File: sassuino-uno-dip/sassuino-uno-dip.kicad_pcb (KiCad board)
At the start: 2 copper layers, 68.6 x 53.3 mm, 33 parts, among them J1 USB_B, J10 OSCPWR_HDR, J2 POWER2_HDR, J3 ICSP_HDR, J4 POWER_HDR, J5 PORTC_HDR, J6 PORTB_HDR, J7 PORTD_HDR, J8 XTAL2_HDR, J9 XTAL1_HDR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

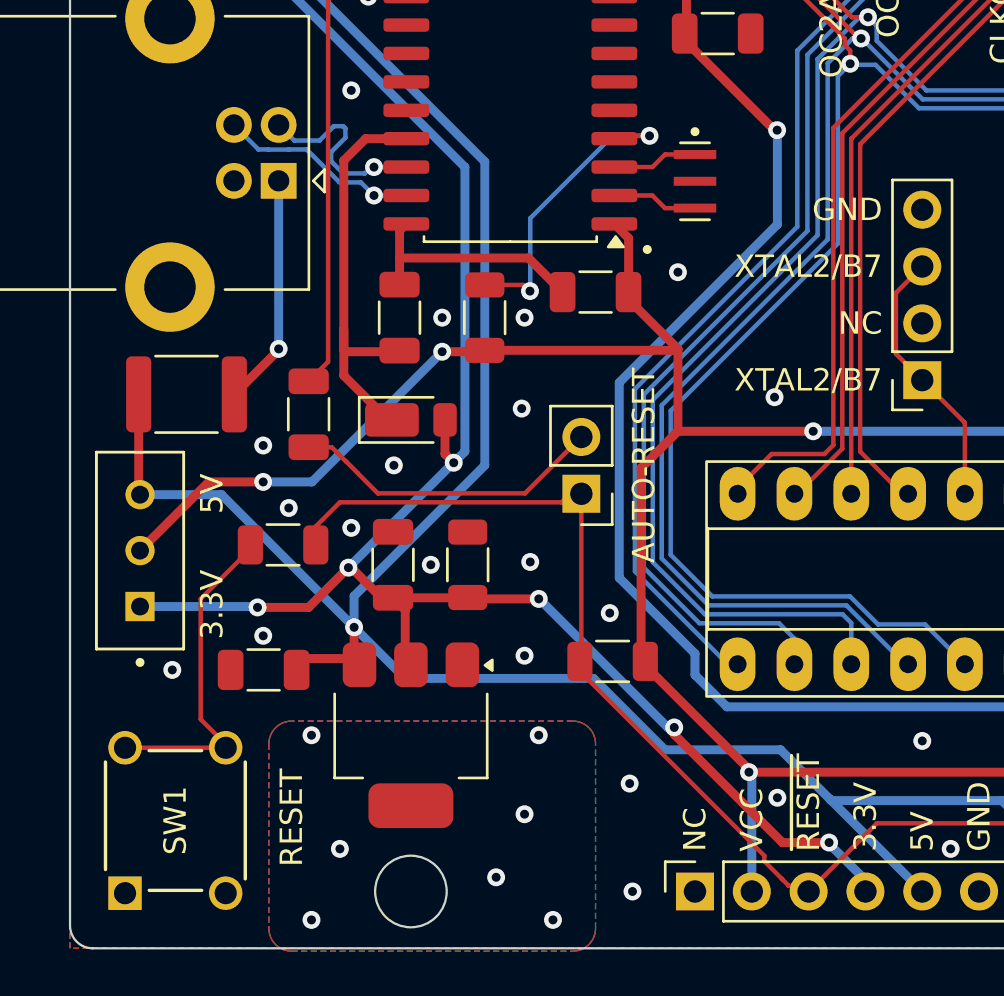
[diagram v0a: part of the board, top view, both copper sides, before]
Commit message: Remove the diode between the two LDOs, I don't remember why it was there.
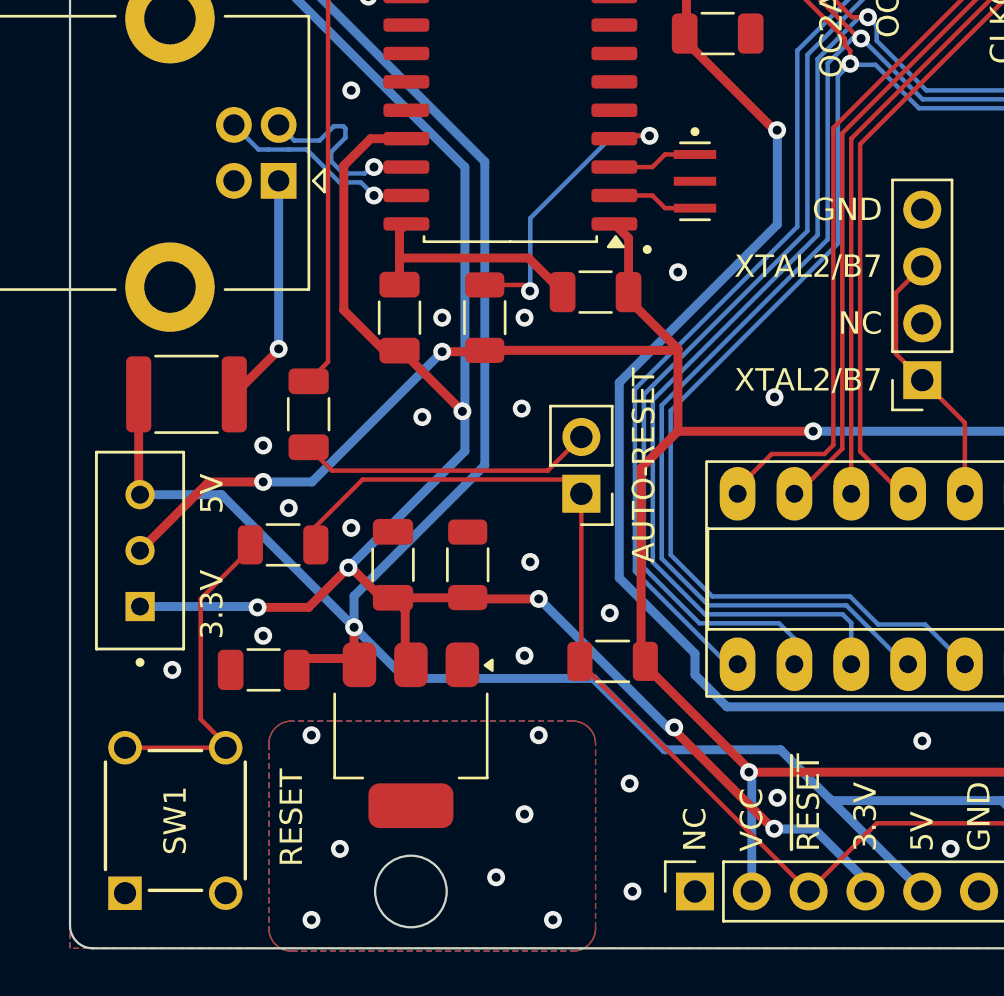
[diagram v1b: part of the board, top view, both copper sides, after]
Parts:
- removed D1: DFLS130L-7, Diode_SMD:D_PowerDI-123
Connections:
- C3 pad 1: /VUSB -> +3.3V
- U2 pad 17: /VUSB -> +3.3V
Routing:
- net /VUSB: track 18.5 -> 0.00 mm
- net +3.3V: track 85.9 -> 100.6 mm
- net Net-(JP2-B): track 14.1 -> 13.2 mm
- net GND: vias 49 -> 48

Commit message: Replace crystal header 3d model with the part I'll likely be using.
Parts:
- J10, J8, J9: footprint Connector_PinSocket_2.54mm:PinSocket_1x04_P2.54mm_Vertical -> 0SassuinoFP:PinSocket_1x04_P2.54mm_Vertical_LowProfile
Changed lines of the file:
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@@
 	(net 50 "/RESET_SW")
 	(net 51 "/VBUS")
-	(footprint "Connector_PinSocket_2.54mm:PinSocket_1x04_P2.54mm_Vertical"
+	(footprint "0SassuinoFP:PinSocket_1x04_P2.54mm_Vertical_LowProfile"
 		(layer "F.Cu")
 		(at 88.9 129.54 180)
@@
 		(tags "Through hole socket strip THT 1x04 2.54mm single row")
 		(property "Reference" "J8"
-			(at 0 10.414 0)
+			(at 0 -2.77 180)
 			(layer "F.SilkS")
-			(hide yes)
 			(effects
 				(font
@@
 		)
 		(property "Value" "XTAL2_HDR"
-			(at 0 10.39 0)
+			(at 0 10.39 180)
 			(layer "F.Fab")
 			(effects
@@
 		)
 		(fp_text user "${REFERENCE}"
-			(at 0 3.81 90)
+			(at 0 3.81 270)
 			(layer "F.Fab")
 			(effects
@@
 		)
 		(embedded_fonts no)
-		(model "${KICAD6_3DMODEL_DIR}/Connector_PinSocket_2.54mm.3dshapes/PinSocket_1x04_P2.54mm_Vertical.wrl"
+		(model "${KIPRJMOD}/../lib/0Sassuino3D/315-47-104-41-001000.STEP"
 			(offset
-				(xyz 0 0 0)
+				(xyz 0 -7.5 3)
 			)
 			(scale
@@
 			)
 			(rotate
-				(xyz 0 0 0)
+				(xyz -90 -0 -90)
 			)
 		)
@@
 		)
 	)
-	(footprint "Connector_PinSocket_2.54mm:PinSocket_1x04_P2.54mm_Vertical"
+	(footprint "0SassuinoFP:PinSocket_1x04_P2.54mm_Vertical_LowProfile"
 		(layer "F.Cu")
 		(at 93.98 129.54 180)
@@
 		(tags "Through hole socket strip THT 1x04 2.54mm single row")
 		(property "Reference" "J9"
-			(at 0 10.414 0)
+			(at 0 -2.77 180)
 			(layer "F.SilkS")
-			(hide yes)
 			(effects
 				(font
@@
 		)
 		(property "Value" "XTAL1_HDR"
-			(at 0 10.39 0)
+			(at 0 10.39 180)
 			(layer "F.Fab")
 			(effects
@@
 		)
 		(fp_text user "${REFERENCE}"
-			(at 0 3.81 90)
+			(at 0 3.81 270)
 			(layer "F.Fab")
 			(effects
@@
 		)
 		(embedded_fonts no)
-		(model "${KICAD6_3DMODEL_DIR}/Connector_PinSocket_2.54mm.3dshapes/PinSocket_1x04_P2.54mm_Vertical.wrl"
+		(model "${KIPRJMOD}/../lib/0Sassuino3D/315-47-104-41-001000.STEP"
 			(offset
-				(xyz 0 0 0)
+				(xyz 0 -7.5 3)
 			)
 			(scale
@@
 			)
 			(rotate
-				(xyz 0 0 0)
+				(xyz -90 -0 -90)
 			)
 		)
 	)
-	(footprint "Connector_PinSocket_2.54mm:PinSocket_1x04_P2.54mm_Vertical"
+	(footprint "0SassuinoFP:PinSocket_1x04_P2.54mm_Vertical_LowProfile"
 		(layer "F.Cu")
 		(at 109.22 129.54 180)
@@
 		(tags "Through hole socket strip THT 1x04 2.54mm single row")
 		(property "Reference" "J10"
-			(at -0.127 10.414 0)
+			(at 0 -2.77 180)
 			(layer "F.SilkS")
-			(hide yes)
 			(effects
 				(font
@@
 		)
 		(property "Value" "OSCPWR_HDR"
-			(at 0 10.39 0)
+			(at 0 10.39 180)
 			(layer "F.Fab")
 			(effects
@@
 		)
 		(fp_text user "${REFERENCE}"
-			(at 0 3.81 90)
+			(at 0 3.81 270)
 			(layer "F.Fab")
 			(effects
@@
 		)
 		(embedded_fonts no)
-		(model "${KICAD6_3DMODEL_DIR}/Connector_PinSocket_2.54mm.3dshapes/PinSocket_1x04_P2.54mm_Vertical.wrl"
+		(model "${KIPRJMOD}/../lib/0Sassuino3D/315-47-104-41-001000.STEP"
 			(offset
-				(xyz 0 0 0)
+				(xyz 0 -7.5 3)
 			)
 			(scale
@@
 			)
 			(rotate
-				(xyz 0 0 0)
+				(xyz -90 -0 -90)
 			)
 		)

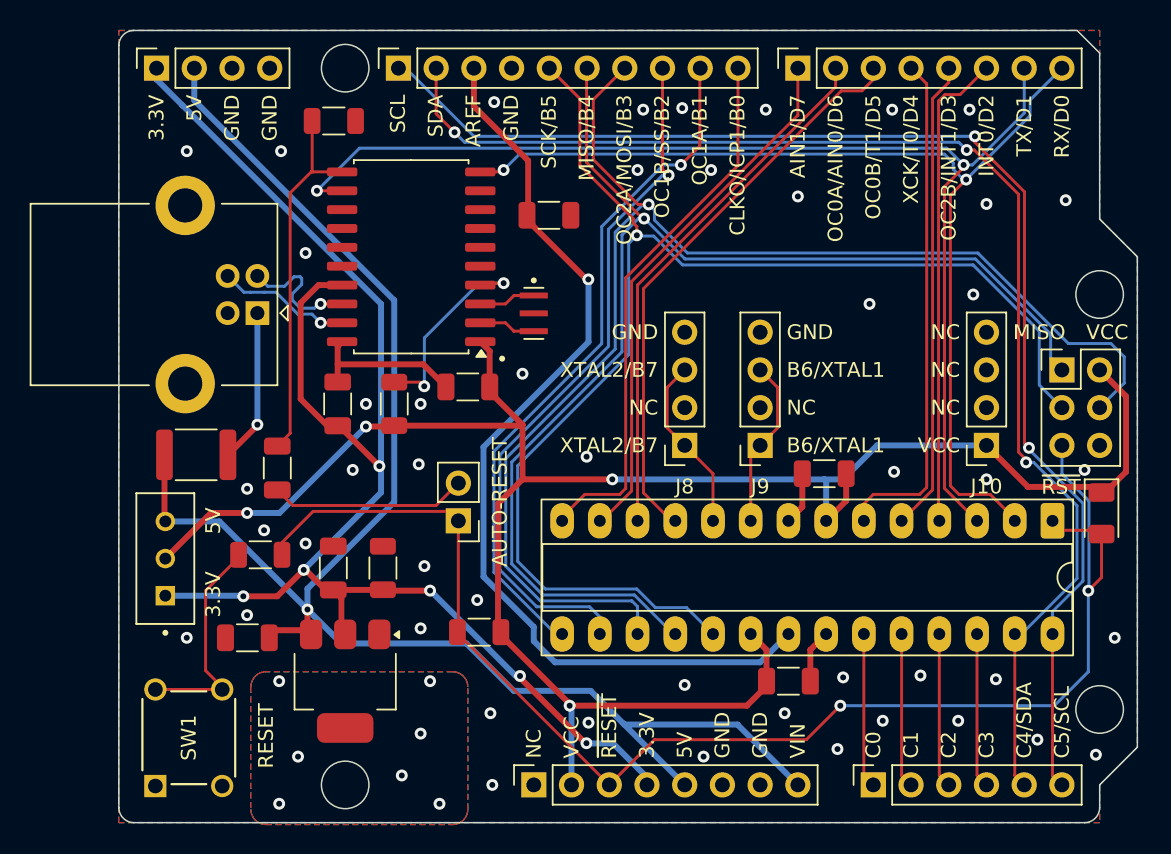
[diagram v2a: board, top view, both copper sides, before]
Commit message: Various cosmetic tweaks.
Switch a few 3d models to the part I'm using.

Update the value of a few symbols to the part number.

Tweak a few traces and silkscreen bits.
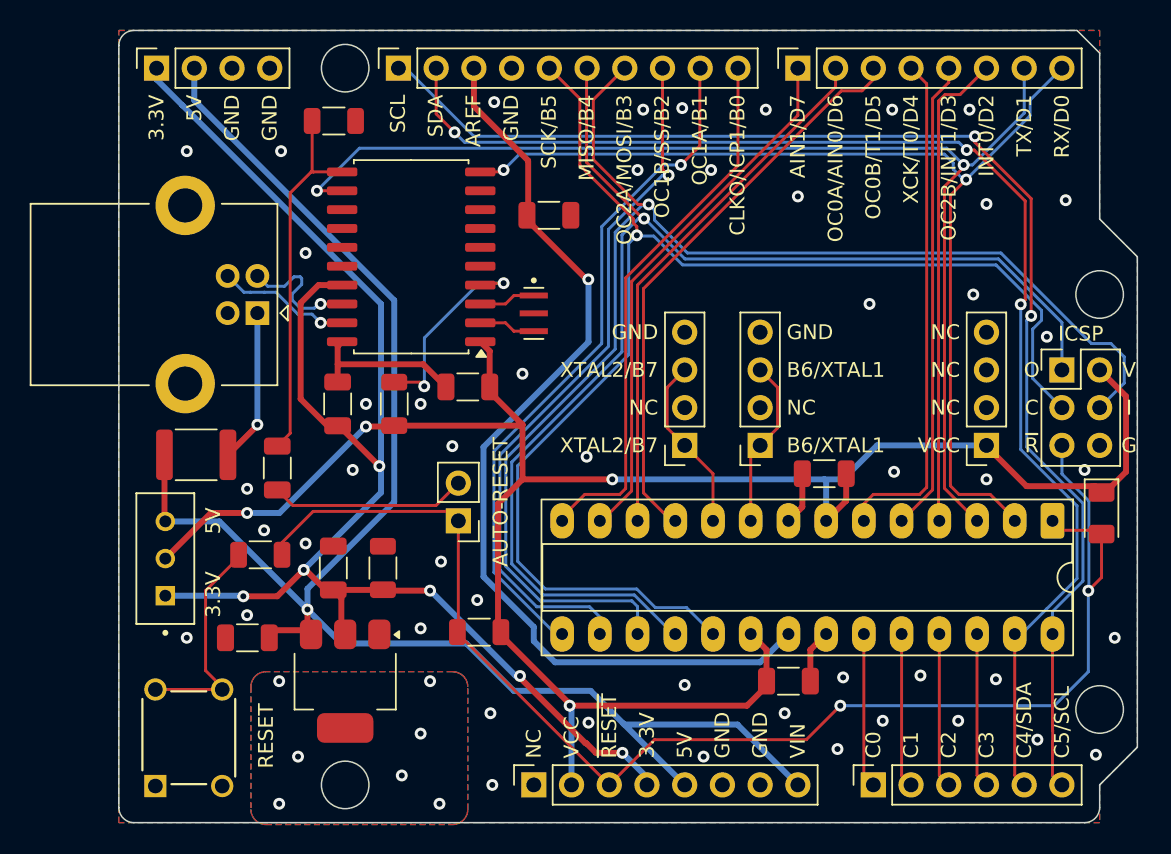
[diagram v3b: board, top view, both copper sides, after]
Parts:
- J10: value OSCPWR_HDR -> 315-47-104-41-001000
- J8: value XTAL2_HDR -> 315-47-104-41-001000
- J9: value XTAL1_HDR -> 315-47-104-41-001000
- SW1: value RESET_SW -> 1825910-7
- SW2: value 5V_33V_SW -> SLW-883935-2A-D
- U1: footprint Package_DIP:DIP-28_W7.62mm_Socket_LongPads -> 0SassuinoFP:DIP-28_W7.62mm_Socket_LongPads
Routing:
- net /PB5/SCK: track 89.7 -> 91.1 mm
- net /PB4/MISO: track 85.1 -> 86.0 mm
- net VCC: track 135.1 -> 135.7 mm
- net GND: vias 48 -> 49
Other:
- board text added: "C"
- board text added: "G"
- board text added: "I"
- board text added: "ICSP"
- board text added: "O"
- board text added: "V"
- board text added: "~{R}"
- board text removed: "MISO"
- board text removed: "~{RST}"

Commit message: Clean up power traces a bit.
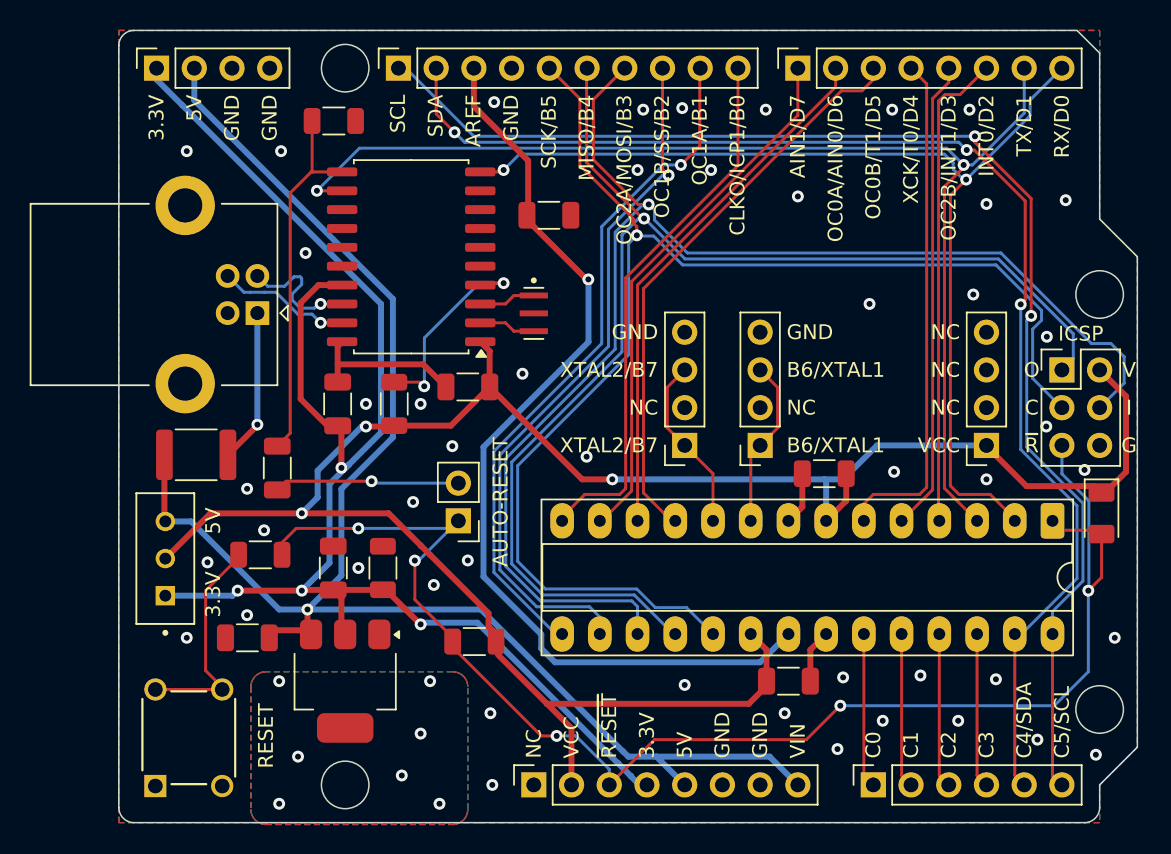
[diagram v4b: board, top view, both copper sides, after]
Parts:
- moved R1 0.71 mm to (74.7, 142.7)
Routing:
- net VCC: track 135.7 -> 139.4 mm, vias 4 -> 3
- net +5V: track 108.4 -> 105.1 mm
- net /~{RESET}: track 93.1 -> 96.1 mm, vias 2 -> 5
- net +3.3V: track 100.6 -> 98.9 mm, vias 13 -> 11
- net Net-(JP2-B): track 13.2 -> 12.5 mm, vias 0 -> 1
- net /PB4/MISO: track 86.0 -> 86.6 mm
- net GND: vias 49 -> 48

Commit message: Move the auto-reset enable header out of the way of shields.
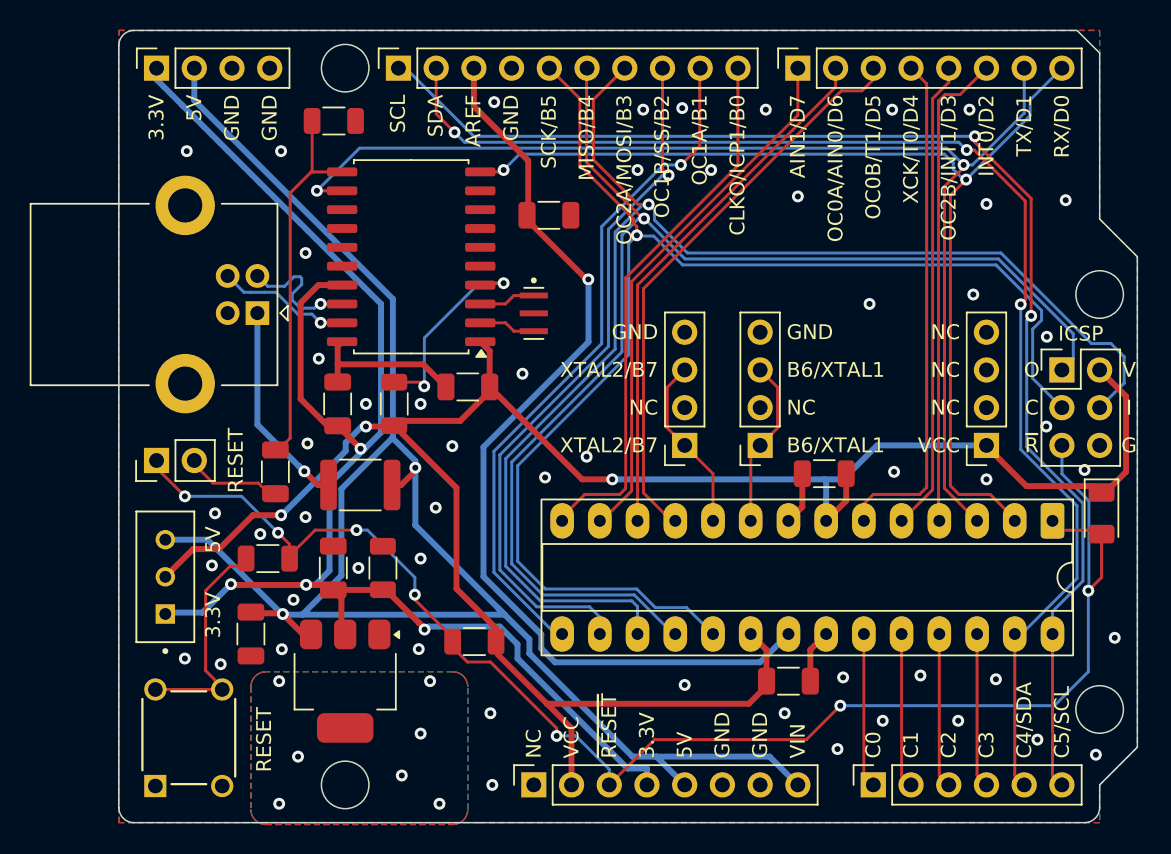
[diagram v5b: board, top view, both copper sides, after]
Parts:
- moved JP2 20.7 mm to (53.3, 130.6), turned to 90 degrees
- moved F1 11.2 mm to (67.1, 132.2), turned to 180 degrees
- moved SW2 1.23 mm to (53.9, 138.4)
- moved R5 0.57 mm to (60.8, 137.2)
- moved C5 0.35 mm to (59.7, 142.2), turned to -90 degrees
- moved C4 0.28 mm to (61.3, 131.3)
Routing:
- net +5V: track 105.1 -> 119.4 mm, vias 1 -> 2
- net Net-(JP2-B): track 12.5 -> 5.85 mm, vias 1 -> 0
- net /~{RESET}: track 96.1 -> 100.8 mm, vias 5 -> 7
- net /VBUS: track 10.4 -> 14.0 mm
- net +3.3V: track 98.9 -> 100.4 mm
- net VCC: track 139.4 -> 138.5 mm
- net GND: vias 48 -> 54
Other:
- board text removed: "AUTO-RESET"

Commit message: Add a couple resistors to protect the MCP2200's TX/RX pins from the MCU.
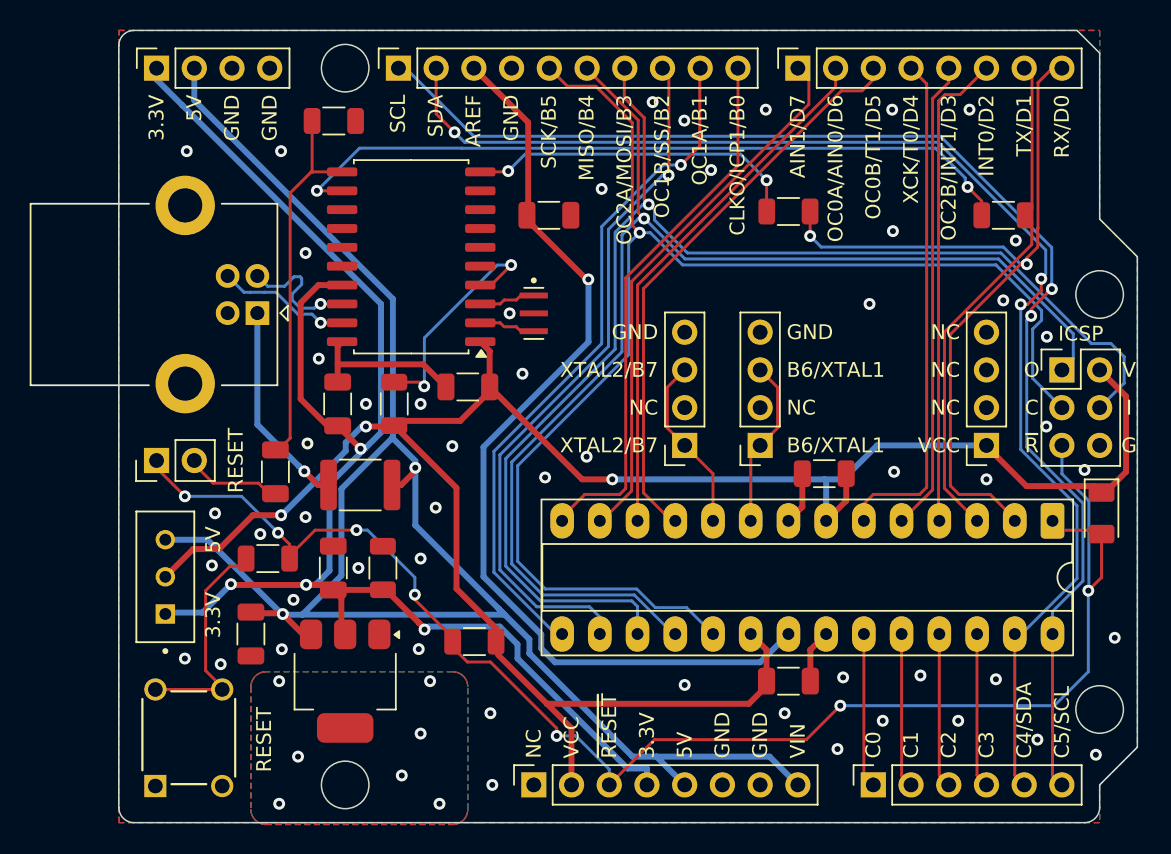
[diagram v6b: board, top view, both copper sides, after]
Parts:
- added R6: 1K, Resistor_SMD:R_1206_3216Metric, F.Cu at (95.9, 113.8)
- added R7: 1K, Resistor_SMD:R_1206_3216Metric, F.Cu at (110.4, 114.0)
- J1: value USB_B -> KUSBEX-BSFS1N-B
- J2: value POWER2_HDR -> PPPC041LFBN-RC
- J4: value POWER_HDR -> PPPC081LFBN-RC
- J5: value PORTC_HDR -> PPPC061LFBN-RC
- J6: value PORTB_HDR -> PPPC101LFBN-RC
- J7: value PORTD_HDR -> PPPC081LFBN-RC
- U1: value ATmega328-P -> ED3050-5-ND
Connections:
- U2 pad 10: /PD0/RXD -> /U_TX
- U2 pad 12: /PD1/TXD -> /U_RX
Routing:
- net /U_RX: track 0.00 -> 50.5 mm, vias 0 -> 2
- net /PD1/TXD: track 80.9 -> 32.4 mm, vias 2 -> 0
- net /U_TX: track 0.00 -> 22.6 mm, vias 0 -> 2
- net /PD0/RXD: track 70.7 -> 53.6 mm
- net /PB3/MOSI: track 92.6 -> 90.4 mm
- net /~{RST}: track 13.7 -> 15.0 mm
- net /PB5/SCK: track 91.1 -> 92.3 mm
- net /PB2: track 48.1 -> 47.5 mm
- net GND: vias 54 -> 53
